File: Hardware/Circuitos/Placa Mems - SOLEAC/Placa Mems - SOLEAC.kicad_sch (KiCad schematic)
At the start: 7 parts, among them J2 Conn_01x04, J6 Conn_01x02, Y1 MA40S4R

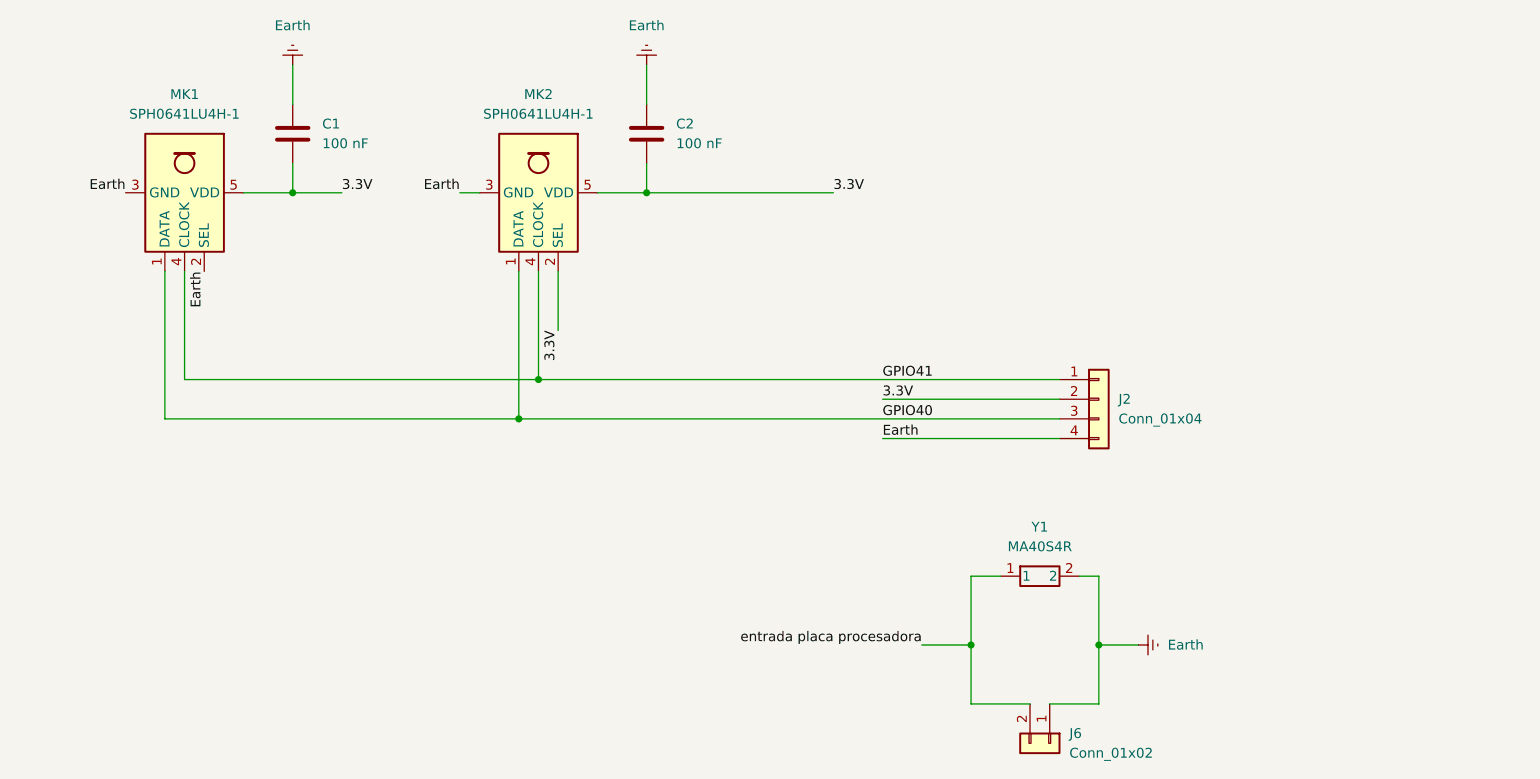
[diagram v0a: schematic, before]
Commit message: Placa Mems - Componentes Mems
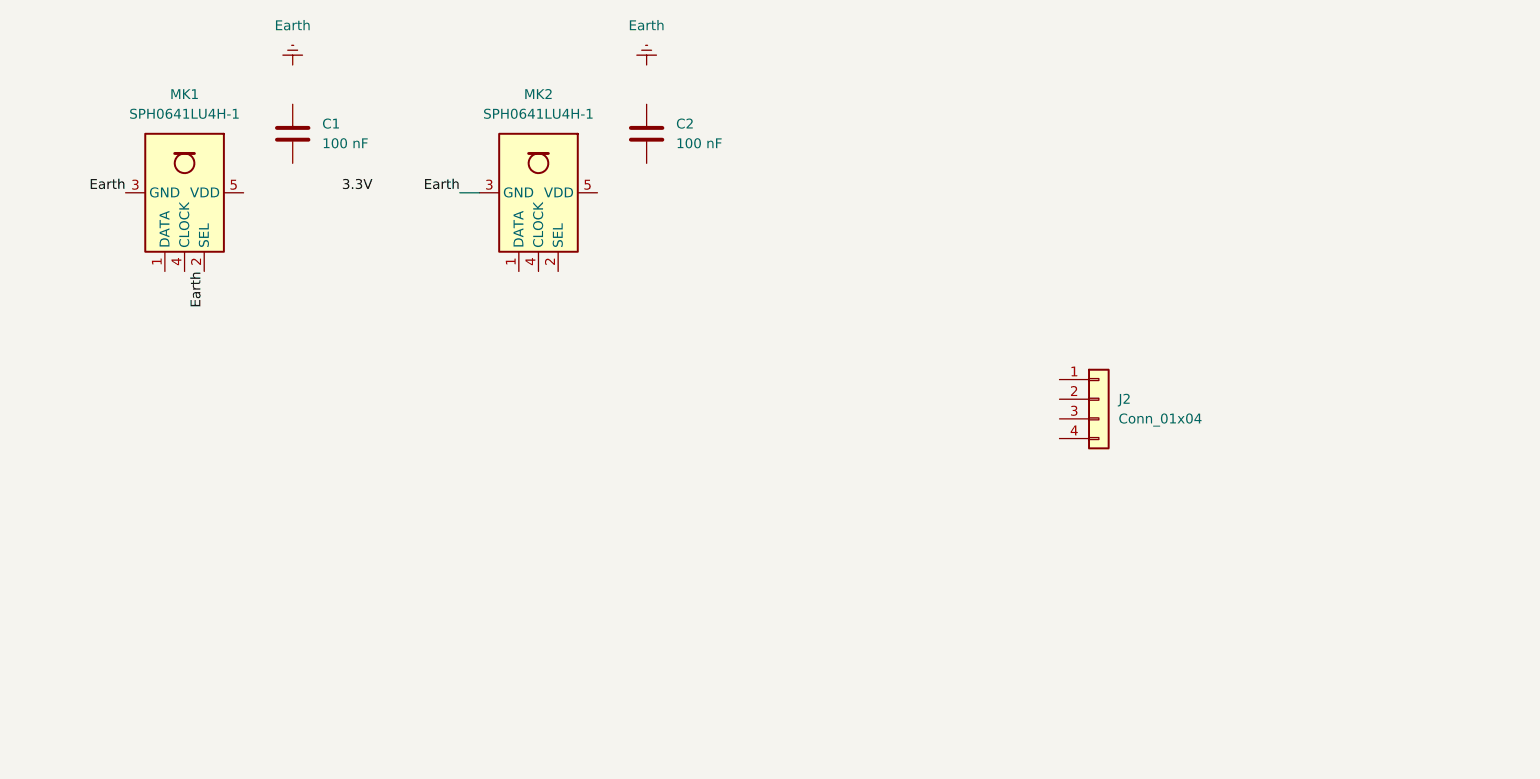
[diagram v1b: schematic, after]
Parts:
- removed J6: Conn_01x02, Connector_Molex:Molex_KK-254_AE-6410-02A_1x02_P2.54mm_Vertical, symbol Connector_Generic:Conn_01x02
- removed Y1: MA40S4R, Murata:MA4024R, symbol Murata:MA4024R
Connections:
- net 3.3V: no longer C1.2, C2.2, J2.2 (Pin_2), MK1.5 (VDD), MK2.2 (SEL), MK2.5 (VDD)
- net Earth: no longer C1.1, C2.1, J2.4 (Pin_4)
- removed net GPIO40: J2.3 (Pin_3), MK1.1 (DATA), MK2.1 (DATA)
- removed net GPIO41: J2.1 (Pin_1), MK1.4 (CLOCK), MK2.4 (CLOCK)

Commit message: Placa Mems - Componentes Murata
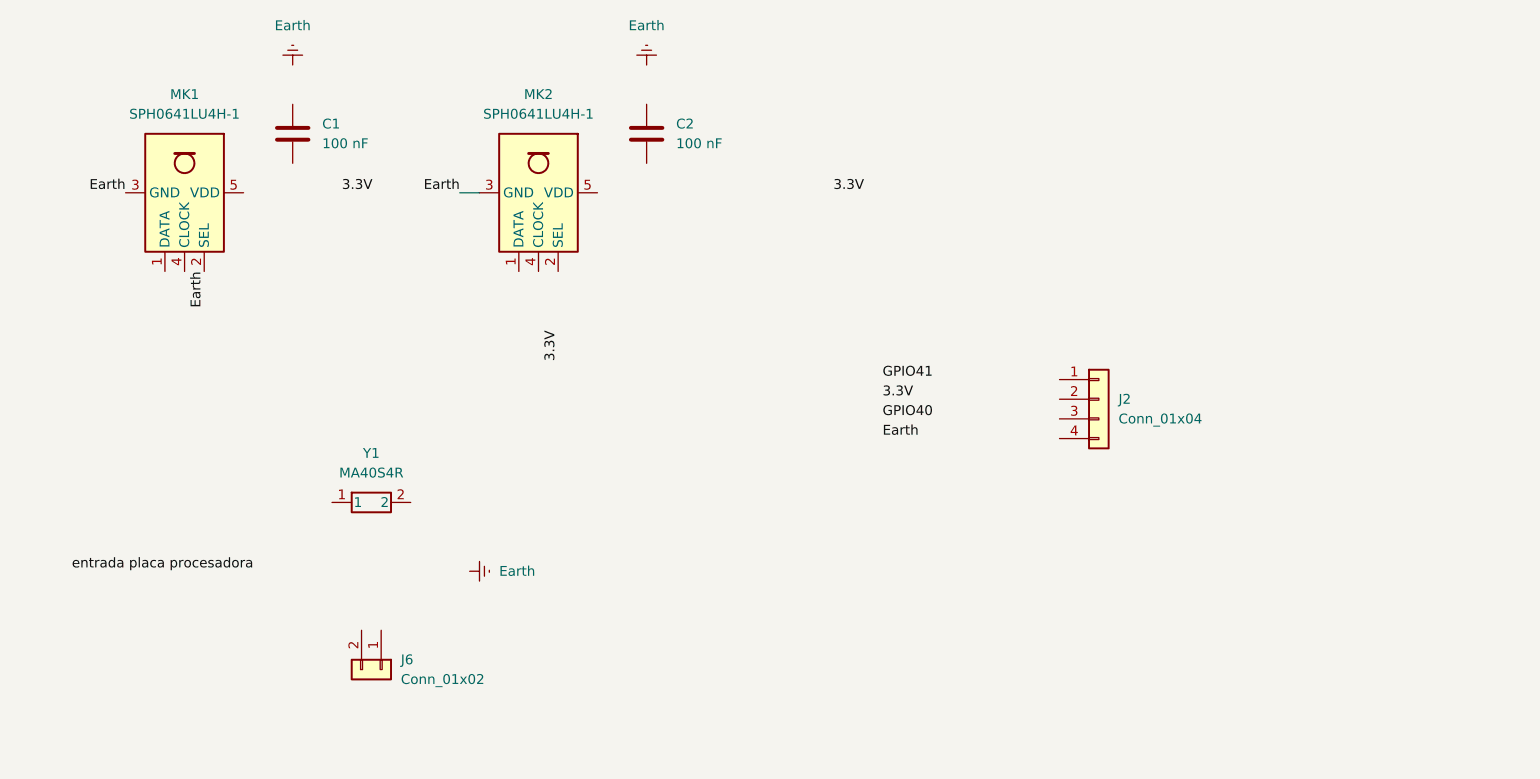
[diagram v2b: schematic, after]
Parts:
- added J6: Conn_01x02, Connector_Molex:Molex_KK-254_AE-6410-02A_1x02_P2.54mm_Vertical, symbol Connector_Generic:Conn_01x02
- added Y1: MA40S4R, Murata:MA4024R, symbol Murata:MA4024R

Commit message: Placa Mems - Conexión componentes
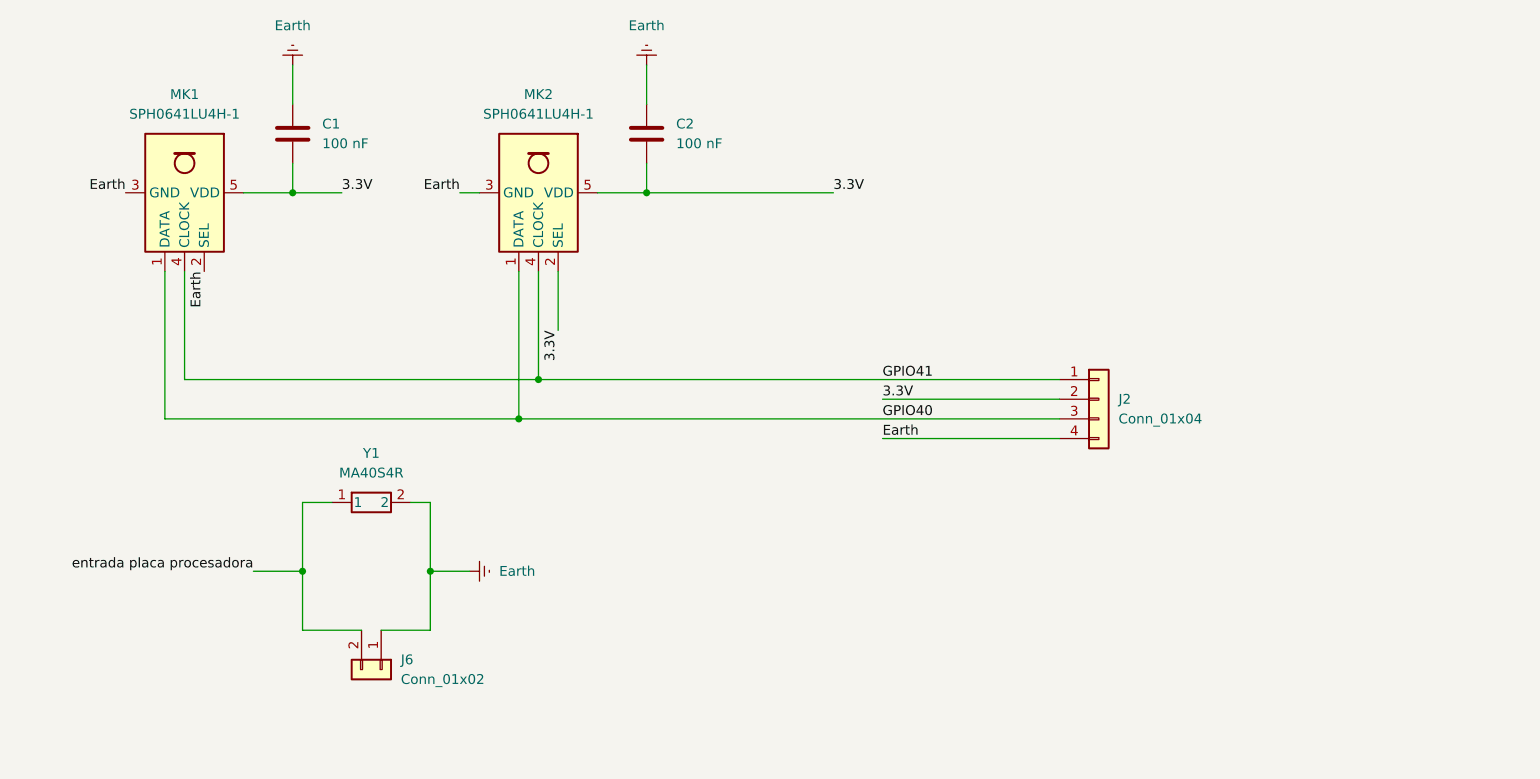
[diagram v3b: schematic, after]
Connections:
- net 3.3V: now also C1.2, C2.2, J2.2 (Pin_2), MK1.5 (VDD), MK2.2 (SEL), MK2.5 (VDD)
- net Earth: now also C1.1, C2.1, J2.4 (Pin_4), J6.1 (Pin_1), Y1.2
- net GPIO40: now also J2.3 (Pin_3), MK1.1 (DATA), MK2.1 (DATA)
- net GPIO41: now also J2.1 (Pin_1), MK1.4 (CLOCK), MK2.4 (CLOCK)
- net entrada placa procesadora: now also J6.2 (Pin_2), Y1.1

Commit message: Placa Mems - Poniendo plug ethernet
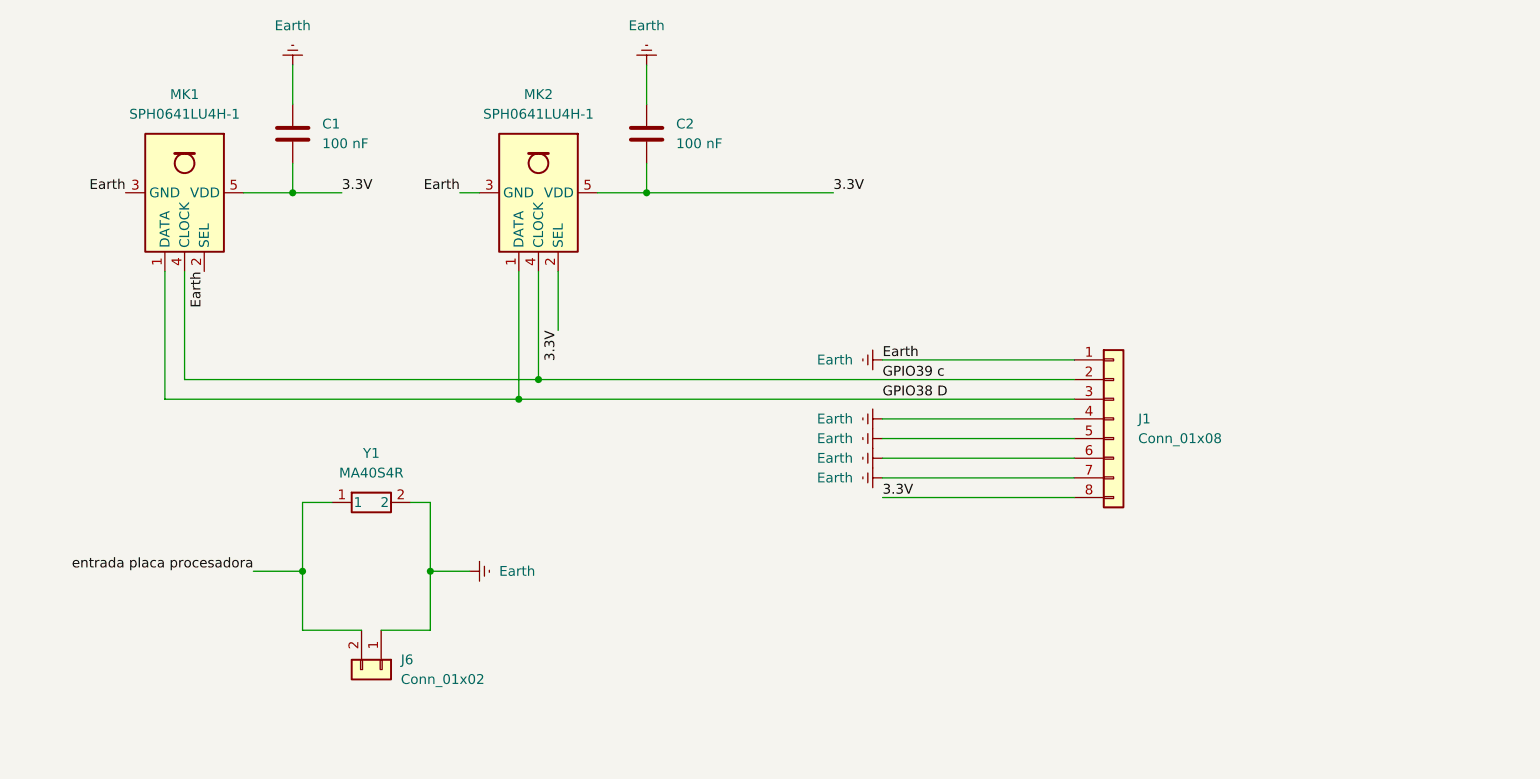
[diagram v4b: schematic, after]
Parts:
- removed J2: Conn_01x04, Connector_Molex:Molex_KK-254_AE-6410-04A_1x04_P2.54mm_Vertical, symbol Connector_Generic:Conn_01x04
- added J1: Conn_01x08, symbol Connector_Generic:Conn_01x08
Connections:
- net 3.3V: now also J1.8 (Pin_8)
- net Earth: now also J1.1 (Pin_1), J1.4 (Pin_4), J1.5 (Pin_5), J1.6 (Pin_6), J1.7 (Pin_7)
- net GPIO40 renamed GPIO38 D
- net GPIO38 D: now also J1.3 (Pin_3)
- net GPIO41 renamed GPIO39 c
- net GPIO39 c: now also J1.2 (Pin_2)

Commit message: Placa Mems- Colocar plug ethernet
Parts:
- J1: footprint (none) -> Connector_RJ:RJ45_Amphenol_54602-x08_Horizontal
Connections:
- net GPIO39 c renamed GPIO39 C
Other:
- moved on the sheet: C1, C2, J1, J6, MK1, MK2, Y1
